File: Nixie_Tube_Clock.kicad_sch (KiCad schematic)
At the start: 9 parts

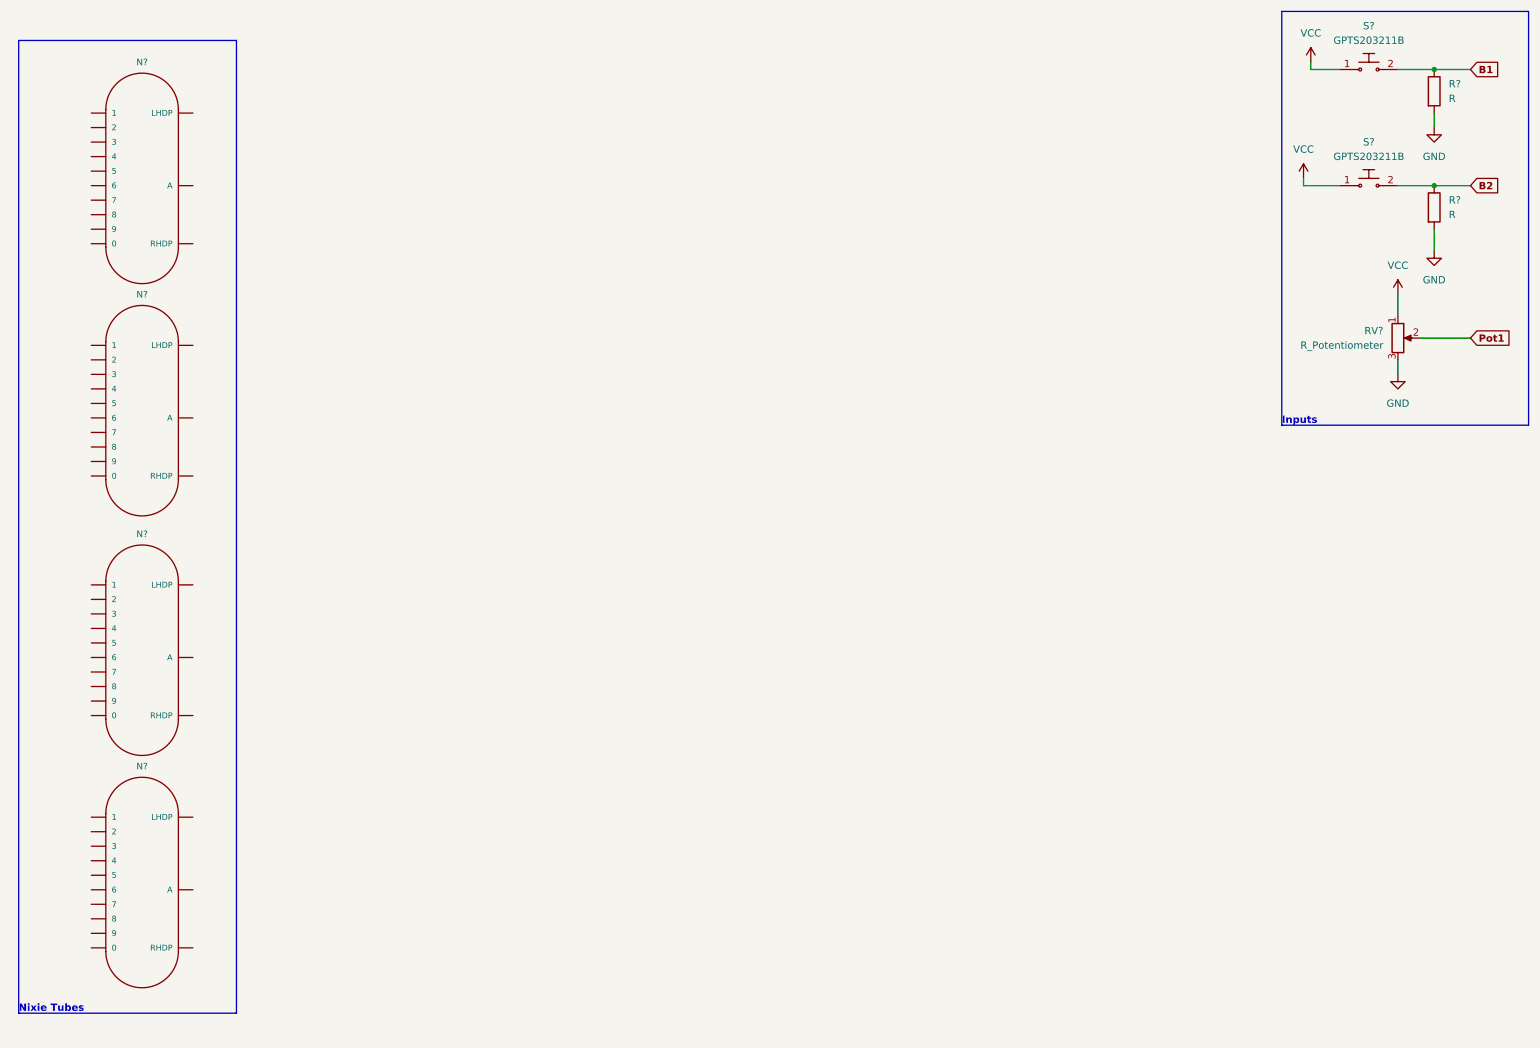
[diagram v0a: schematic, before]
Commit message: Added several subcircuits
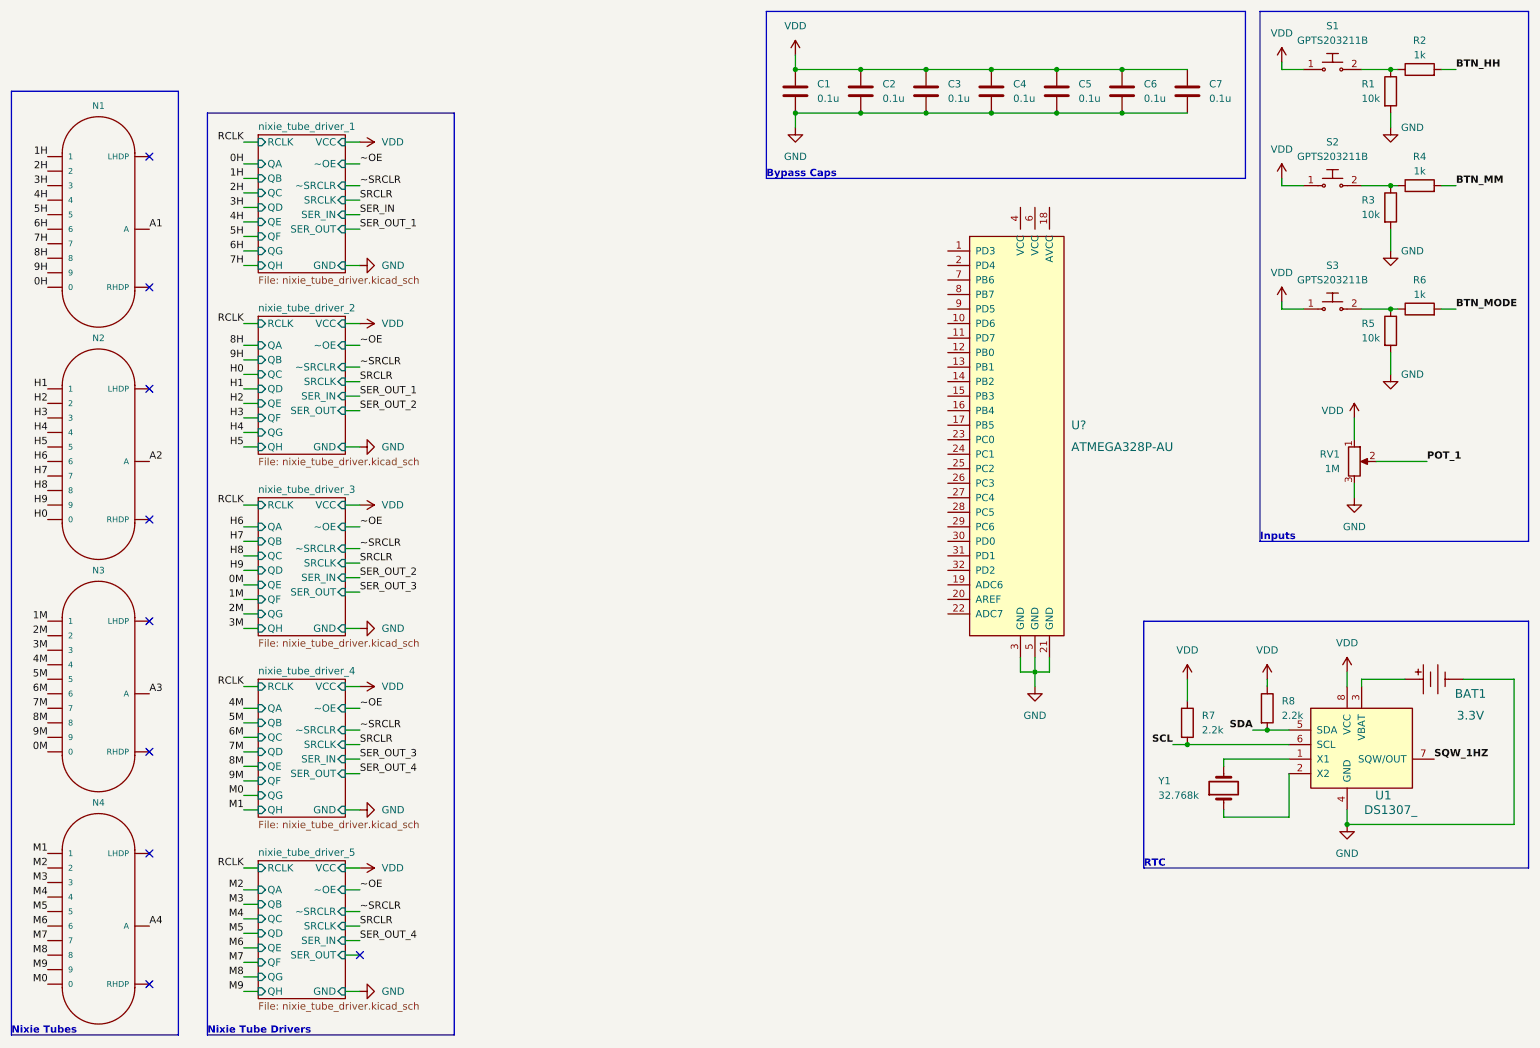
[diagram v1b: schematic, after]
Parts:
- added BAT1: 3.3V, digikey-footprints:Battery_Holder_Coin_2032_BS-7, symbol dk_Battery-Holders-Clips-Contacts:BS-7
- added C1, C2, C3, C4, C5, C6, C7: 0.1u, symbol Device:C
- added R2, R4, R6: 1k, symbol Device:R
- added R5: 10k, symbol Device:R
- added R7, R8: 2.2k, symbol Device:R
- added S3: GPTS203211B, digikey-footprints:PushButton_12x12mm_THT_GPTS203211B, symbol dk_Pushbutton-Switches:GPTS203211B
- added U1: DS1307_, digikey-footprints:DIP-8_W7.62mm, symbol dk_Clock-Timing-Real-Time-Clocks:DS1307_
- added U?: ATMEGA328P-AU, digikey-footprints:TQFP-32_7x7mm, symbol dk_Embedded-Microcontrollers:ATMEGA328P-AU
- added Y1: 32.768k, symbol Device:Crystal
- R1, R3: renamed from R?; value R -> 10k
- RV1: renamed from RV?; value R_Potentiometer -> 1M
- gave numbers to parts that had none: 6
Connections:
- net GND: now also BAT1.Neg, C1.2, C2.2, C3.2, C4.2, C5.2, C6.2, C7.2, R5.2, U1.4 (GND), U?.21 (GND), U?.3 (GND), U?.5 (GND)
- net M0: now reaches N4.0
- net M1: now reaches N4.1
- net M2: now reaches N4.2
- net M3: now reaches N4.3
- net M4: now reaches N4.4
- net M5: now reaches N4.5
- net M6: now reaches N4.6
- net M7: now reaches N4.7
- net M8: now reaches N4.8
- net M9: now reaches N4.9
- net A4: now reaches N4.A
- net 0M: now reaches N3.0
- net 1M: now reaches N3.1
- net 2M: now reaches N3.2
- net 3M: now reaches N3.3
- net 4M: now reaches N3.4
- net 5M: now reaches N3.5
- net 6M: now reaches N3.6
- net 7M: now reaches N3.7
- net 8M: now reaches N3.8
- net 9M: now reaches N3.9
- net A3: now reaches N3.A
- net 0H: now reaches N1.0
- net 1H: now reaches N1.1
- net 2H: now reaches N1.2
- net 3H: now reaches N1.3
- net 4H: now reaches N1.4
- net 5H: now reaches N1.5
- net 6H: now reaches N1.6
- net 7H: now reaches N1.7
- net 8H: now reaches N1.8
- net 9H: now reaches N1.9
- net A1: now reaches N1.A
- net H0: now reaches N2.0
- net H1: now reaches N2.1
- net H2: now reaches N2.2
- net H3: now reaches N2.3
- net H4: now reaches N2.4
- net H5: now reaches N2.5
- net H6: now reaches N2.6
- net H7: now reaches N2.7
- net H8: now reaches N2.8
- net H9: now reaches N2.9
- net A2: now reaches N2.A
- net B1: no longer names the net of R1.1, S1.2
- net B1: now also R2.1
- net B2: no longer names the net of R3.1, S2.2
- net B2: now also R4.1
- net Pot1 renamed POT_1
- net VCC renamed VDD
- net VDD: now also C1.1, C2.1, C3.1, C4.1, C5.1, C6.1, C7.1, R7.1, R8.1, S3.1, U1.8 (VCC)
- new net: R5.1, R6.1, S3.2
- new net: BAT1.Pos, U1.3 (VBAT)
- new net: U1.1 (X1), Y1.2
- new net: U1.2 (X2), Y1.1
- new net BTN_HH: R2.2
- new net BTN_MM: R4.2
- new net BTN_MODE: R6.2
- new net SCL: R7.2, U1.6 (SCL)
- new net SDA: R8.2, U1.5 (SDA)
- new net SQW_1HZ: U1.7 (SQW/OUT)
- no-connect marks 0 -> 9
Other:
- added sheet nixie_tube_driver_1 (nixie_tube_driver.kicad_sch)
- added sheet nixie_tube_driver_2 (nixie_tube_driver.kicad_sch)
- added sheet nixie_tube_driver_3 (nixie_tube_driver.kicad_sch)
- added sheet nixie_tube_driver_4 (nixie_tube_driver.kicad_sch)
- added sheet nixie_tube_driver_5 (nixie_tube_driver.kicad_sch)
- note added: "Bypass Caps"
- note added: "Nixie Tube Drivers"
- note added: "RTC"
- moved on the sheet: N1, N2, N3, N4, R1, R3, RV1, S1, S2
